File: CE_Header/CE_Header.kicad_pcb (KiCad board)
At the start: 2 copper layers, 53.3 x 53.3 mm, 4 parts

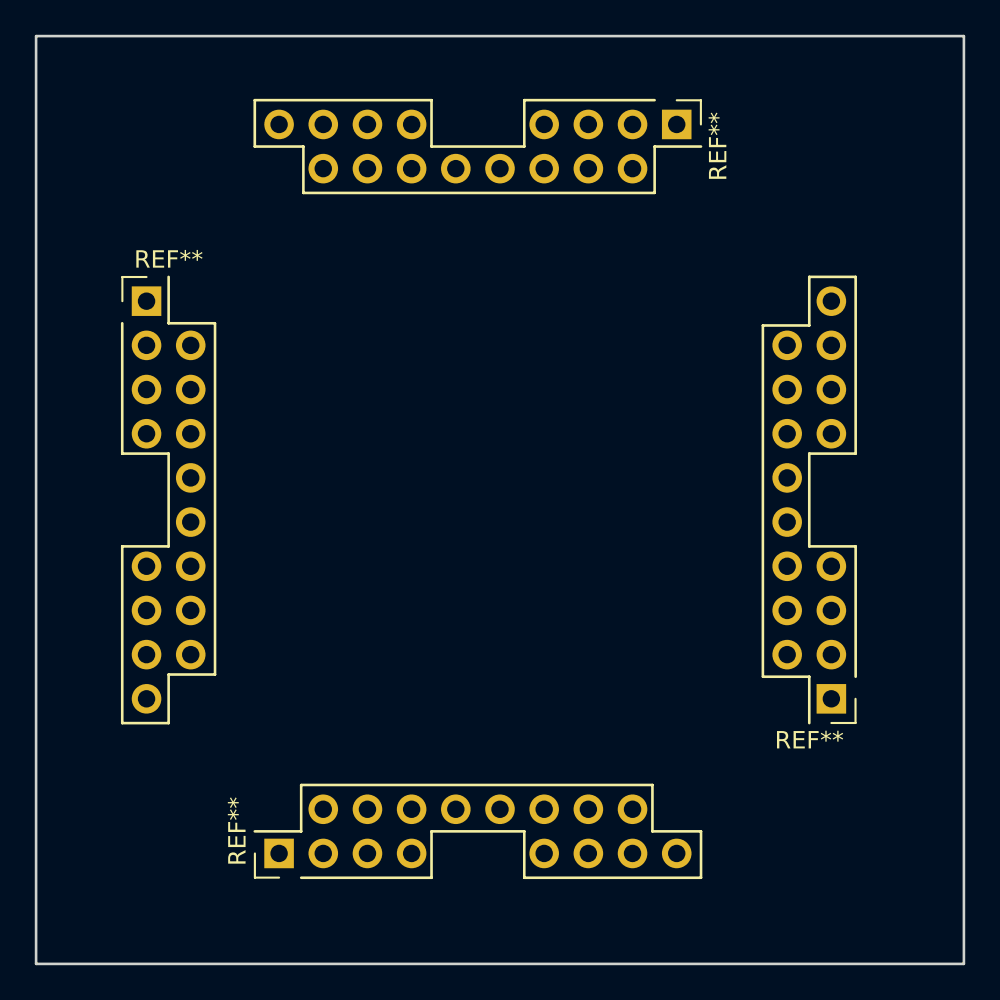
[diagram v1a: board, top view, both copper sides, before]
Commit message: Added the socket to complement the header
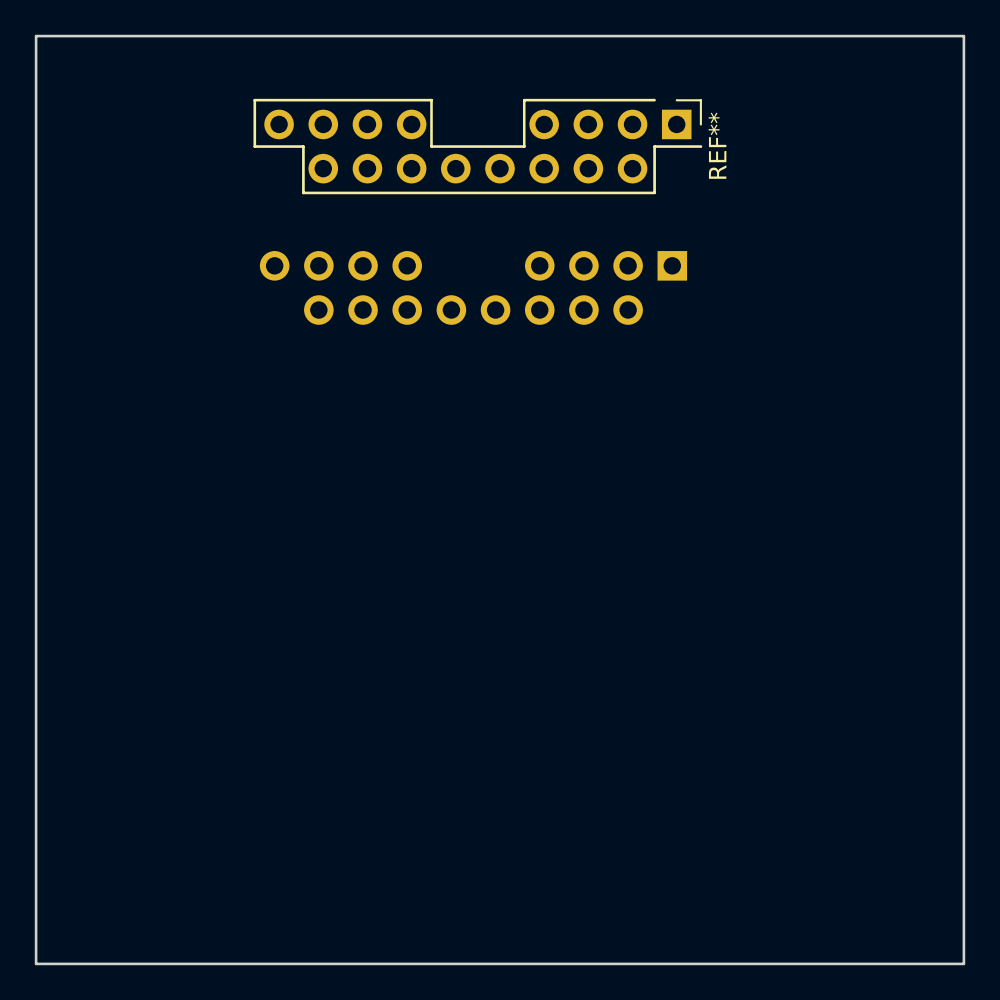
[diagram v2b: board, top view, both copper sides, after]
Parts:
- removed the REF** at (180.3, 101.6)
- removed the REF** at (148.6, 110.5)
- removed the REF** at (141.0, 78.7)
- added REF**: CE_Socket, CE_Header:CE_Socket, B.Cu at (171.2, 79.2)
